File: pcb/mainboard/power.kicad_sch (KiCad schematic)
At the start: 77 parts, among them SW1 EVQPUJ02K, U1 AXP209, U100 MCIMX6Y7DVM09AB, U2 SY7208, U3 SY8008

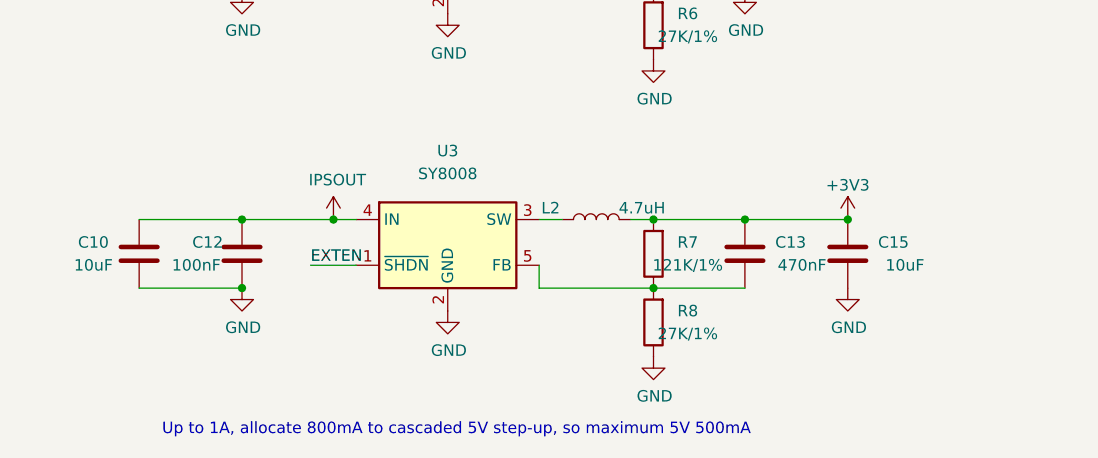
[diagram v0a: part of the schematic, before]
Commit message: pcb: switch to max17135, length tuning for QSPI and SD
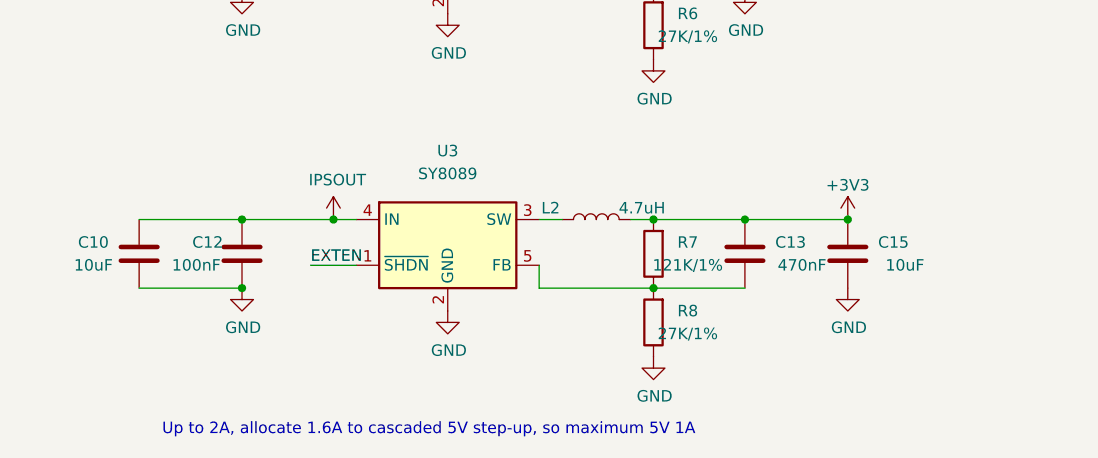
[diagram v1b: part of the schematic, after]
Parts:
- U3: value SY8008 -> SY8089
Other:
- note added: "Up to 2A, allocate 1.6A to cascaded 5V step-up, so maximum 5V 1A"
- note removed: "Up to 1A, allocate 800mA to cascaded 5V step-up, so maximum 5V 500mA"
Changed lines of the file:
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@@
     (stroke (width 0) (type solid) (color 0 0 0 0))
   )
-  (text "Up to 1A, allocate 800mA to cascaded 5V step-up, so maximum 5V 500mA"
+  (text "Up to 2A, allocate 1.6A to cascaded 5V step-up, so maximum 5V 1A"
     (at 60.96 195.58 0)
     (effects (font (size 1.27 1.27)) (justify left bottom))
@@
     (in_bom yes) (on_board yes) (fields_autoplaced)
     (property "Reference" "U3" (id 0) (at 92.71 163.83 0))
-    (property "Value" "SY8008" (id 1) (at 92.71 166.37 0))
+    (property "Value" "SY8089" (id 1) (at 92.71 166.37 0))
     (property "Footprint" "Package_TO_SOT_SMD:TSOT-23-5" (id 2) (at 93.345 180.34 0)
       (effects (font (size 1.27 1.27) italic) (justify left) hide)
